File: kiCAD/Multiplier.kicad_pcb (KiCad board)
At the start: 2 copper layers, 59 parts, among them IC2 ADG1221BRMZ, J1 Conn_01x02_Pin, J2 Conn_01x02_Pin, J3 Conn_01x02_Pin, Q7 Q_Dual_PNP_PNP_C1B1B2C2E2E1, Q8 Q_Dual_PNP_PNP_C1B1B2C2E2E1, U1 TS912, U10 TPS63060, U2 TLV340, U4 TS912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

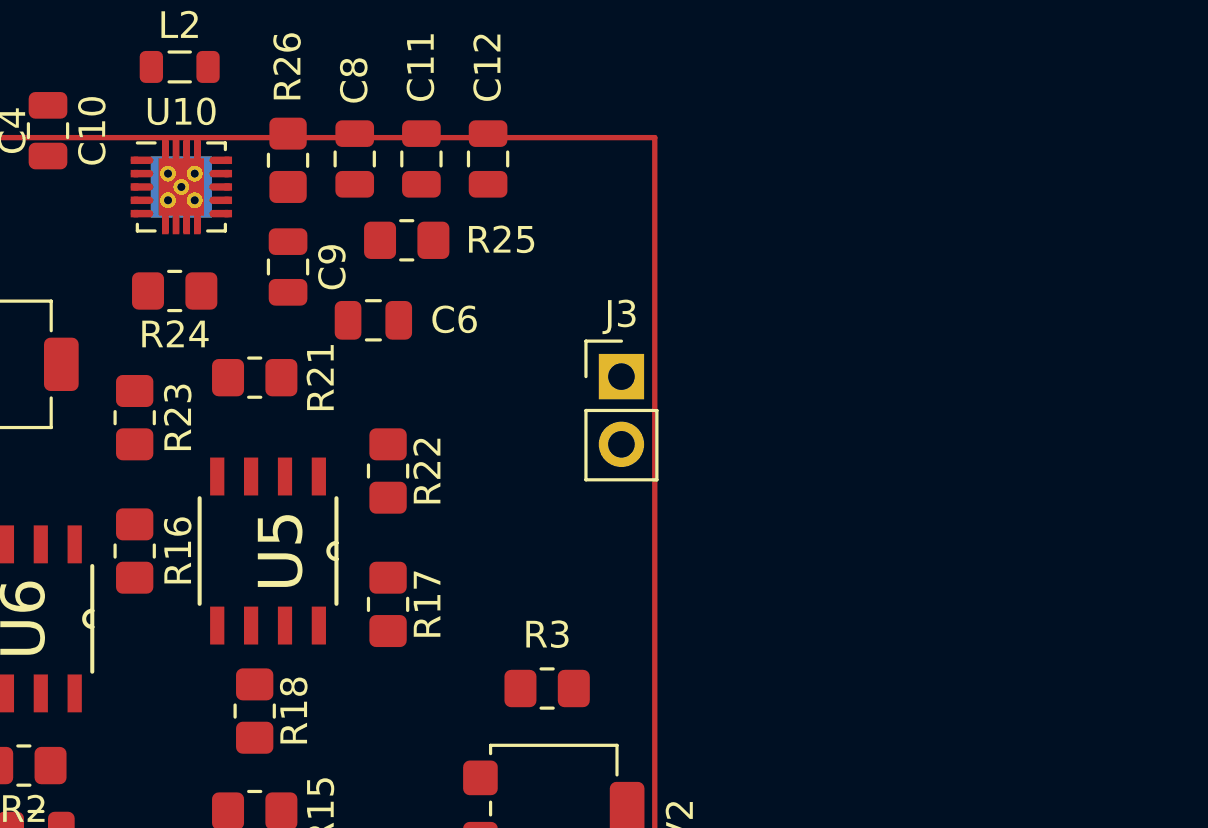
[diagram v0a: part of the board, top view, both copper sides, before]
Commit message: Add tantalum cap footprint
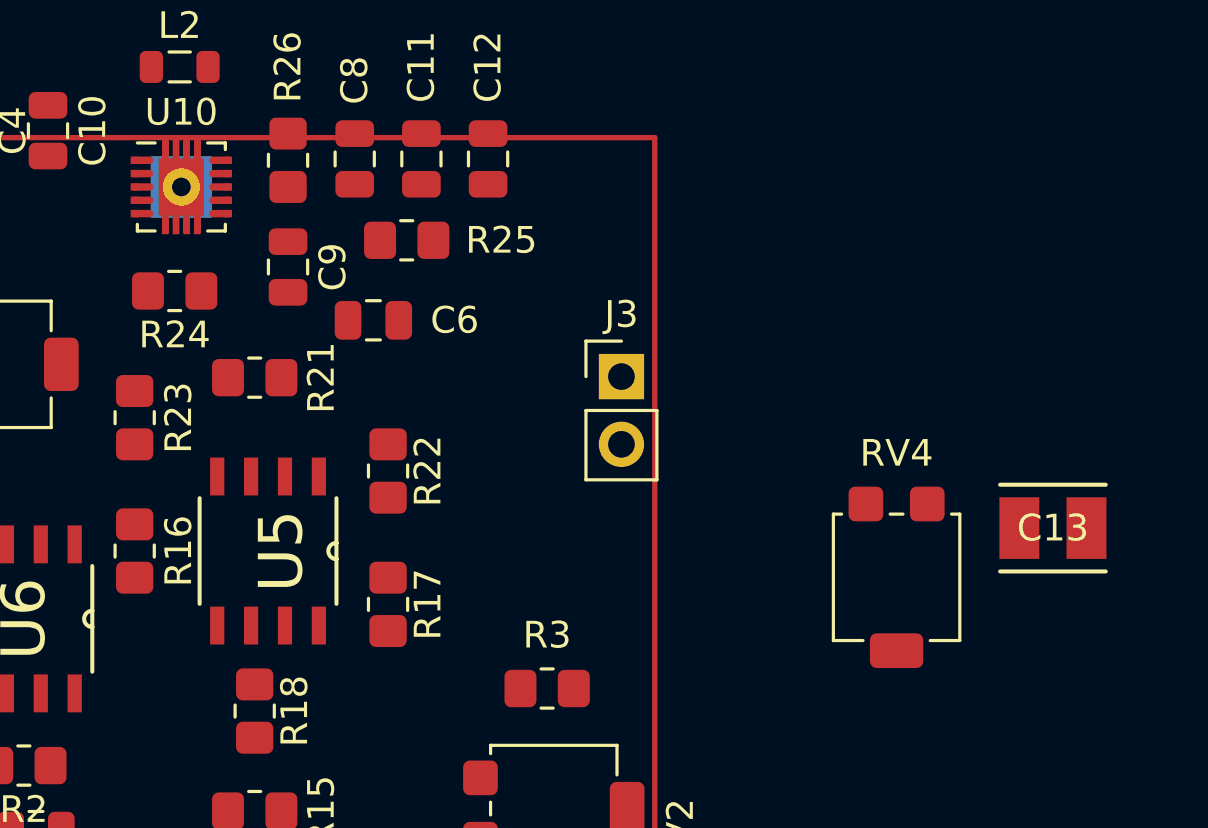
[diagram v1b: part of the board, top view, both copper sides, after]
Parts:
- added C13: 100n, Custom:CAP_293D-B_VSS, F.Cu at (153.4, 104.1)
- added RV4: 3k, Potentiometer_SMD:Potentiometer_Bourns_3314G_Vertical, F.Cu at (147.6, 106.0)
- R22: value 3k -> 7,5k
- R3: value 25k -> 24k
- RV1: value 1,1k -> 1,15k
- RV2: value 12k -> 12,5k
- RV3: value 1,1k -> 2,4k
- U10: footprint Package_SON:Texas_S-PWSON-N10_ThermalVias -> Custom:Texas_S-PWSON-N10_ThermalVias_Custom
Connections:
- R22 pad 2: Net-(U5A--) -> Net-(R22-Pad2)
